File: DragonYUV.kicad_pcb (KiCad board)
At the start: 4 copper layers, 120 x 64.1 mm, 68 parts, among them IC1 74HCT273, IC10 74HCT32, IC12 CD4053, IC2 MC6847, IC3 74HCT00, IC4 74HCT20, IC5 74HCT86, IC6 74HCT393, IC7 74ALS74N, IC8 74HCT393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

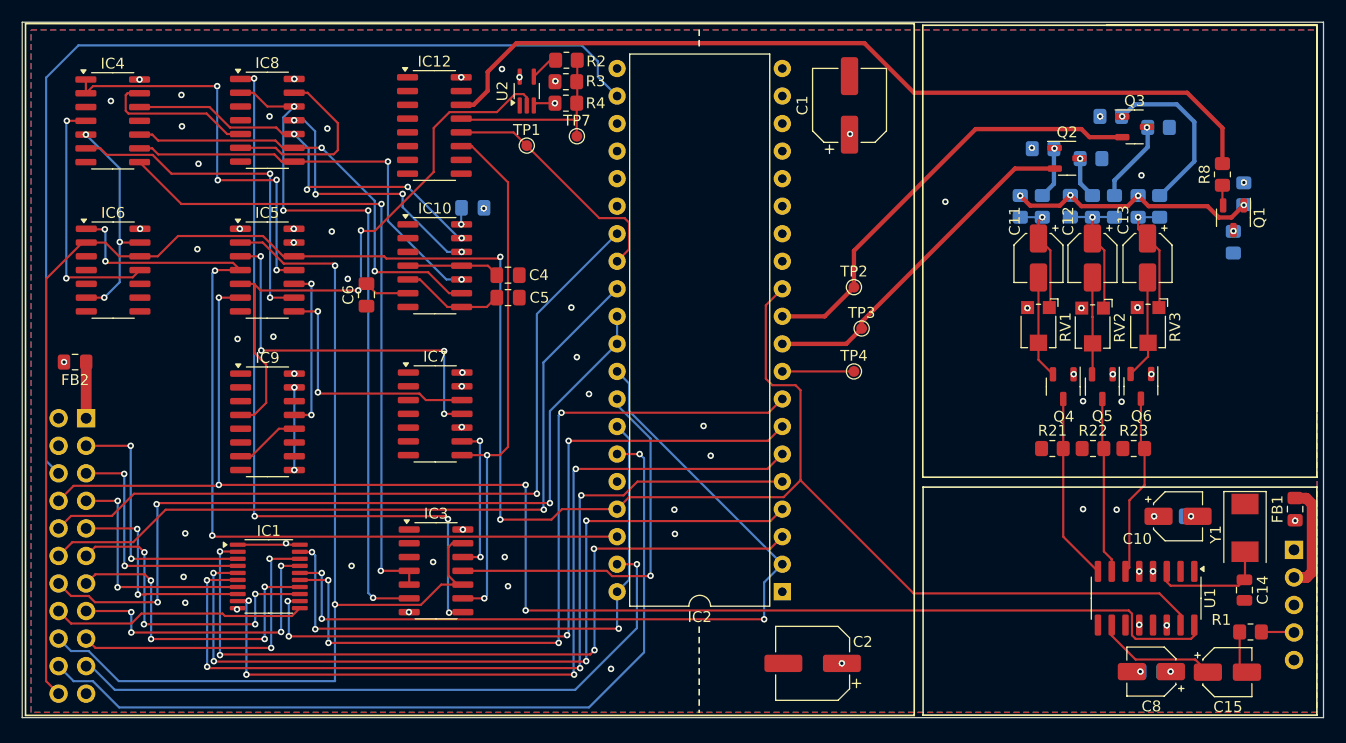
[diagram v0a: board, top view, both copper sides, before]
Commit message: reworked layout
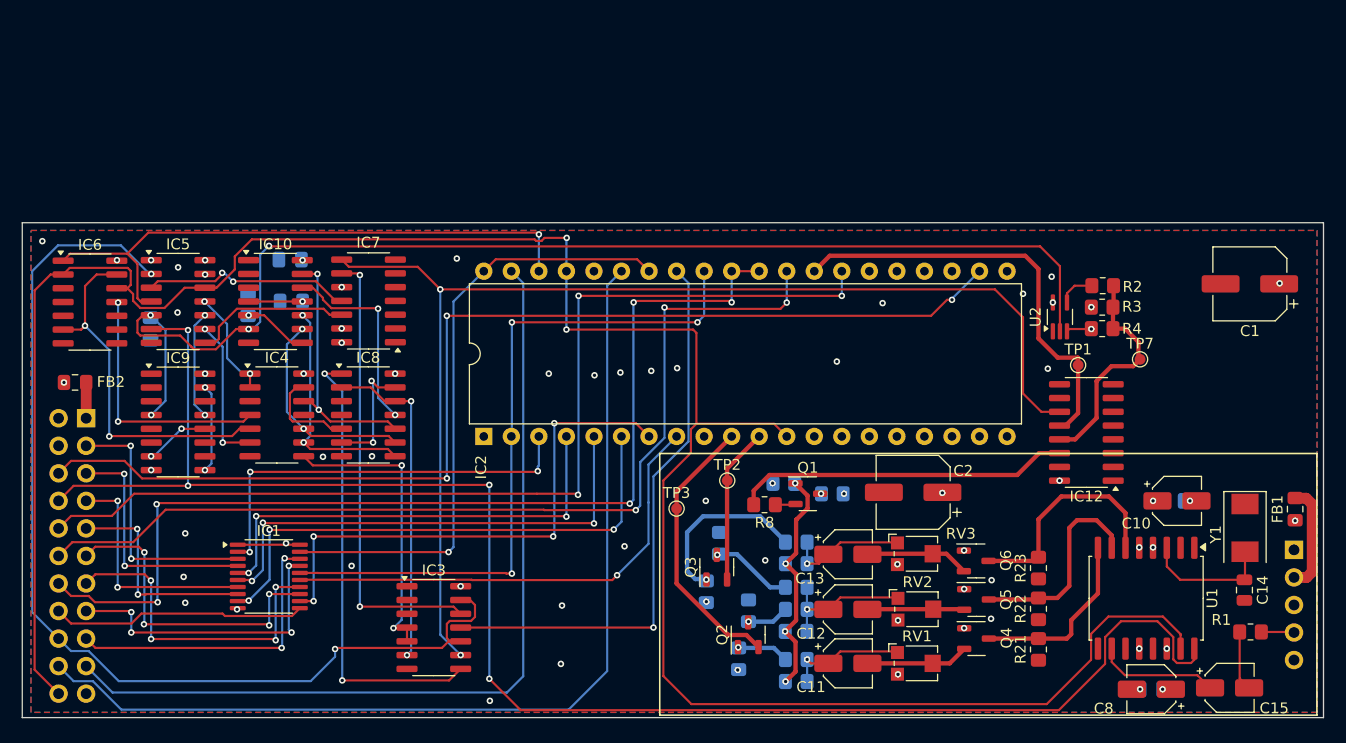
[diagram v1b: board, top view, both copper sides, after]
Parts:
- removed TP4: TestPoint_Chroma, TestPoint:TestPoint_Pad_D1.0mm
- C4, C5, C6: moved to B.Cu
- U1: footprint Package_SO:SOIC-16_3.9x9.9mm_P1.27mm -> Package_SO:SOIC-16W_7.5x10.3mm_P1.27mm
- moved IC12 66.5 mm to (188.2, 100.8), turned to 180 degrees
- moved R12 57.6 mm to (153.1, 115.5), turned to -90 degrees
- moved Q3 56.0 mm to (154.1, 113.3), turned to 90 degrees
- moved TP7 55.9 mm to (193.1, 94.1)
- moved R13 55.8 mm to (154.3, 111.0), turned to -90 degrees
- moved R10 54.8 mm to (156.1, 121.7), turned to -90 degrees
- moved TP1 54.7 mm to (187.4, 94.6)
- moved R3 53.7 mm to (189.6, 89.3)
- moved R4 53.7 mm to (189.6, 91.3)
- moved R2 53.7 mm to (189.7, 87.3)
- moved U2 53.4 mm to (185.7, 90.2)
- moved Q2 52.9 mm to (157.0, 119.5), turned to 90 degrees
- moved R11 52.3 mm to (157.0, 117.3), turned to -90 degrees
- moved R8 52.1 mm to (158.5, 107.5), turned to 180 degrees
- moved R7 50.1 mm to (160.3, 105.5), turned to 180 degrees
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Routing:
- net LUM CONTROL: track 50.0 -> 110.6 mm
- net /LINE PULSES: track 60.1 -> 113.0 mm, vias 2 -> 4
- net MUX X: track 80.1 -> 30.9 mm
- net /Q0: track 73.4 -> 38.3 mm, vias 4 -> 3
- net /Q2: track 80.4 -> 45.7 mm, vias 4 -> 3
- net Net-(IC3-Pad4): track 61.7 -> 27.3 mm
- net /Q1: track 76.3 -> 42.6 mm, vias 4 -> 3
- net Net-(IC8A-MR): track 62.6 -> 30.5 mm, vias 4 -> 2
- net Net-(IC7B-Q): track 14.0 -> 41.9 mm
- net /Q3: track 76.9 -> 49.0 mm, vias 4 -> 3
- net /~{VCLK}: track 69.6 -> 41.9 mm, vias 4 -> 2
- net Net-(IC4-Pad1): track 37.7 -> 10.1 mm, vias 4 -> 2
- net ~{HS}: track 81.8 -> 54.3 mm, vias 4 -> 1
- net /Q5: track 71.9 -> 44.5 mm, vias 4 -> 1
- net phiA: track 40.8 -> 14.4 mm
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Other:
- board size 120 x 64.1 mm -> 120 x 45.6 mm

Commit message: Clean up board Improve trace quality
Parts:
- added TP4: TestPoint_MuxX, TestPoint:TestPoint_Pad_D1.0mm, F.Cu at (180.7, 104.7)
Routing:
- net DO6: track 28.1 -> 30.8 mm
- net CLK: track 52.4 -> 50.7 mm
- net /LINE PULSES: track 113.0 -> 114.3 mm
- net ~{RAS0}: track 23.5 -> 24.8 mm
- net VCLK: track 96.8 -> 95.8 mm
- net DO7: track 28.2 -> 29.0 mm
- net ~{FS}: track 213.6 -> 214.5 mm
- net DO5: track 30.6 -> 31.4 mm
- net DO4: track 29.9 -> 30.6 mm
- net LUM: track 39.9 -> 40.4 mm, vias 0 -> 1
- net GM0: track 95.9 -> 95.3 mm
- net GM1: track 89.3 -> 88.7 mm
- net GND: vias 38 -> 48
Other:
- board text added: "DRAGON REV.3 PAL"

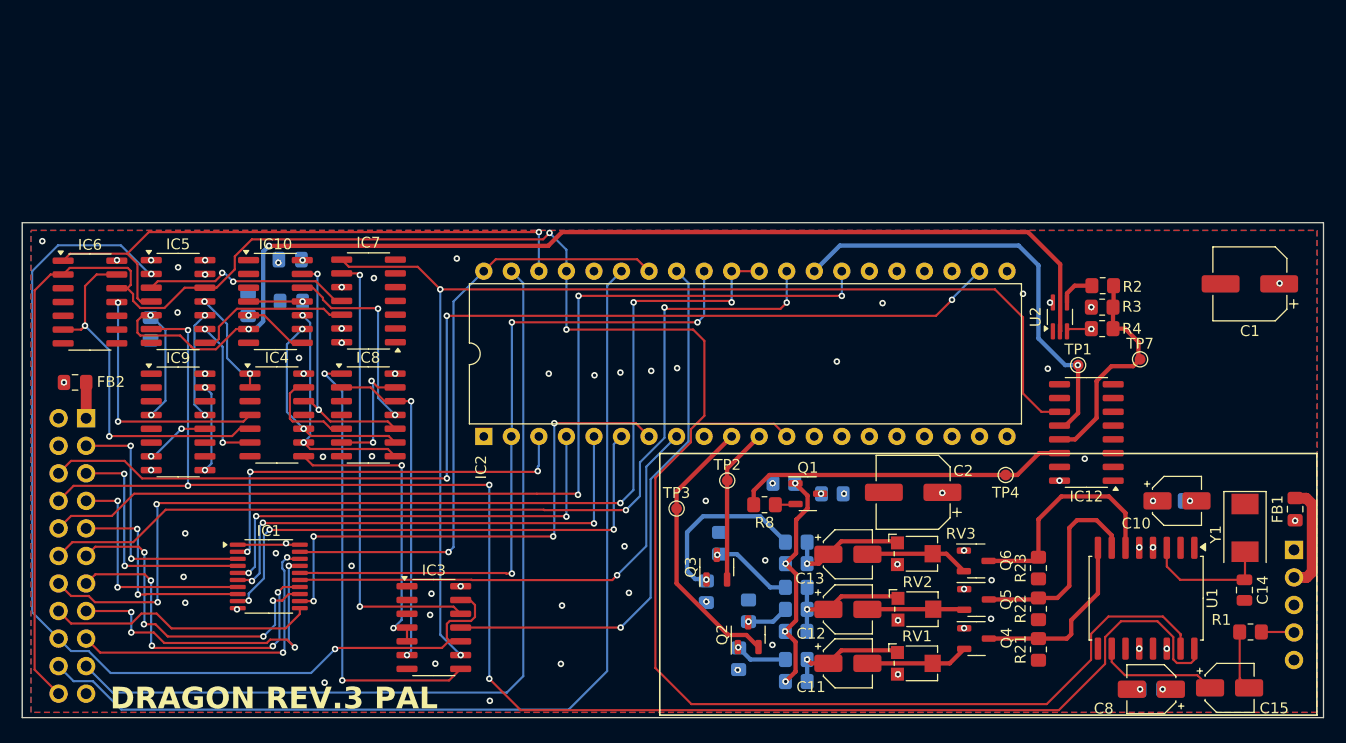
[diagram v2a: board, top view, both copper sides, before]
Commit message: bolster video output routing
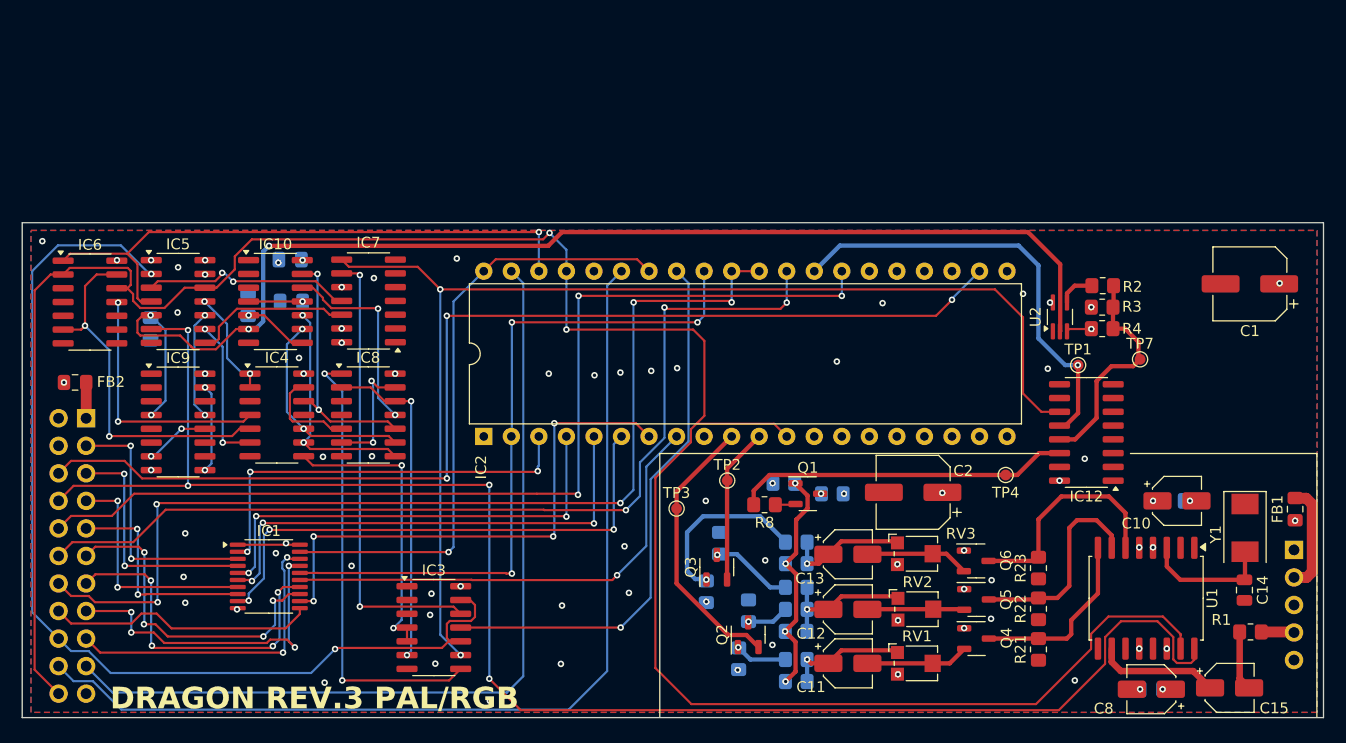
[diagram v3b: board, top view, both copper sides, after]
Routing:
- net ~{FS}: track 214.5 -> 213.9 mm
- net GND: vias 48 -> 49
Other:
- board text added: "DRAGON REV.3 PAL/RGB"
- board text removed: "DRAGON REV.3 PAL"

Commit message: convert to cpld
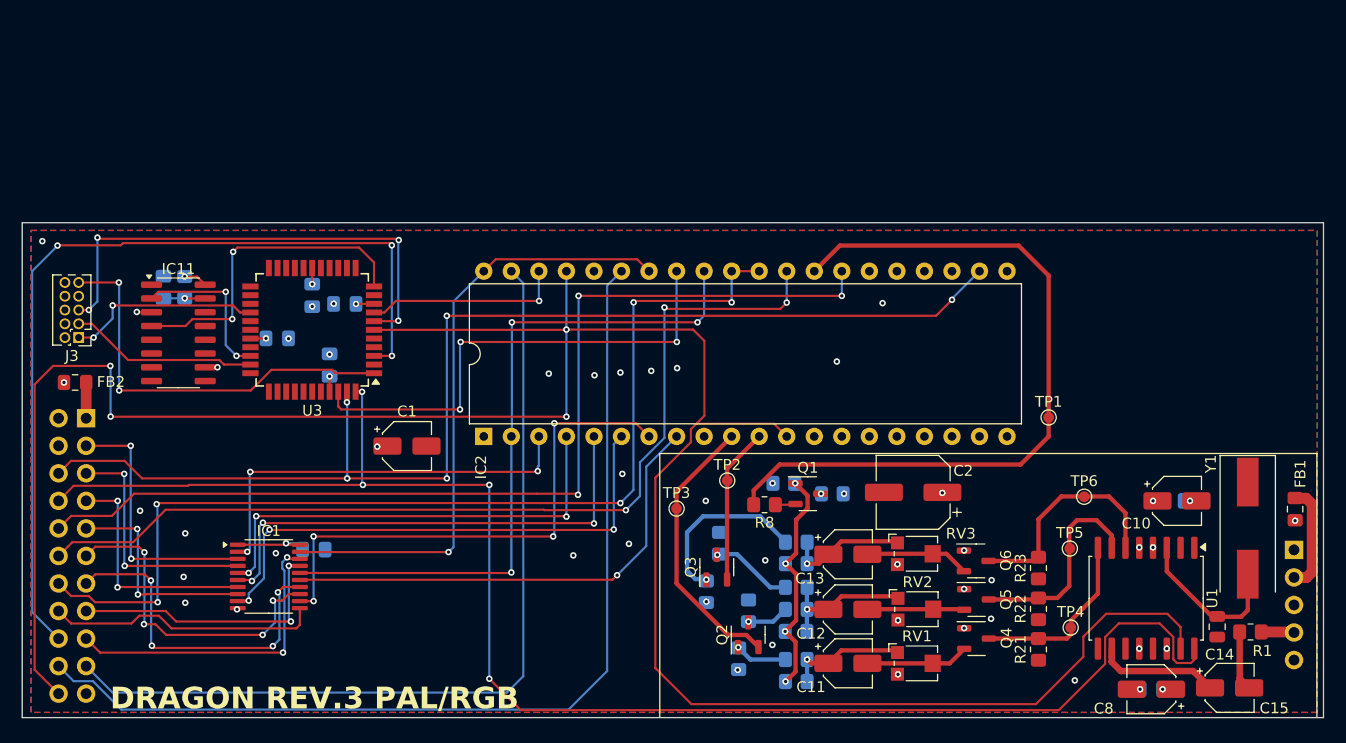
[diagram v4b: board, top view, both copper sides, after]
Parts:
- removed C5: 100pF, Capacitor_SMD:C_0805_2012Metric_Pad1.18x1.45mm_HandSolder
- removed C6: 180pF, Capacitor_SMD:C_0805_2012Metric_Pad1.18x1.45mm_HandSolder
- removed C9: 0.01uF, Capacitor_SMD:C_0805_2012Metric_Pad1.18x1.45mm_HandSolder
- removed IC10: 74HCT32, Package_SO:SOIC-14_3.9x8.7mm_P1.27mm
- removed IC12: CD4053, Package_SO:SOIC-16_3.9x9.9mm_P1.27mm
- removed IC3: 74HCT00, Package_SO:SOIC-14_3.9x8.7mm_P1.27mm
- removed IC4: 74HCT20, Package_SO:SOIC-14_3.9x8.7mm_P1.27mm
- removed IC5: 74HCT86, Package_SO:SOIC-14_3.9x8.7mm_P1.27mm
- removed IC6, IC8: 74HCT393, Package_SO:SOIC-14_3.9x8.7mm_P1.27mm
- removed IC7: 74ALS74N, Package_SO:SOIC-14_3.9x8.7mm_P1.27mm
- removed IC9: 74HCT390, Package_SO:SOIC-16_3.9x9.9mm_P1.27mm
- removed R2: 12K, Resistor_SMD:R_0805_2012Metric_Pad1.20x1.40mm_HandSolder
- removed R3: 8K2, Resistor_SMD:R_0805_2012Metric_Pad1.20x1.40mm_HandSolder
- removed R4: 1K8, Resistor_SMD:R_0805_2012Metric_Pad1.20x1.40mm_HandSolder
- removed TP7: TestPoint_LinePulse, TestPoint:TestPoint_Pad_D1.0mm
- removed U2: 74AHC1G04, Package_TO_SOT_SMD:SOT-353_SC-70-5_Handsoldering
- added C16: 0.1uF, Capacitor_SMD:C_0805_2012Metric_Pad1.18x1.45mm_HandSolder, B.Cu at (116.8, 88.2)
- added C17: 0.1uF, Capacitor_SMD:C_0805_2012Metric_Pad1.18x1.45mm_HandSolder, B.Cu at (113.5, 92.2)
- added C18: 0.1uF, Capacitor_SMD:C_0805_2012Metric_Pad1.18x1.45mm_HandSolder, B.Cu at (118.4, 94.6)
- added C19: 0.1uF, Capacitor_SMD:C_0805_2012Metric_Pad1.18x1.45mm_HandSolder, B.Cu at (119.8, 89.0)
- added C20: 330pF, Capacitor_SMD:C_0805_2012Metric_Pad1.18x1.45mm_HandSolder, B.Cu at (103.0, 87.5)
- added IC11: 74LS123N, Package_SO:SOIC-16_3.9x9.9mm_P1.27mm, F.Cu at (104.4, 91.6)
- added J3: JTAG, Connector_PinHeader_1.27mm:PinHeader_2x05_P1.27mm_Vertical, F.Cu at (95.2, 92.1)
- added R5: 27K, Resistor_SMD:R_0805_2012Metric_Pad1.20x1.40mm_HandSolder, B.Cu at (105.0, 87.5)
- added TP5: TestPoint_Green, TestPoint:TestPoint_Pad_D1.0mm, F.Cu at (186.6, 111.5)
- added TP6: TestPoint_Blue, TestPoint:TestPoint_Pad_D1.0mm, F.Cu at (188.0, 106.8)
- added U3: ATF1504ASL-xAx44, Package_QFP:TQFP-44_10x10mm_P0.8mm, F.Cu at (116.8, 91.4)
- C1: footprint Capacitor_SMD:CP_Elec_6.3x5.8 -> Capacitor_SMD:CP_Elec_4x5.4
- C14: value 52pF -> 51pF
- C4: value 180pF -> 0.1uF
- TP4: value TestPoint_MuxX -> TestPoint_Blue
- Y1: footprint Crystal:Crystal_SMD_0603-2Pin_6.0x3.5mm -> Crystal:Crystal_SMD_HC49-SD
- moved C1 79.2 mm to (125.5, 102.1), turned to 0 degrees
- moved C4 23.0 mm to (116.9, 111.6)
- moved TP4 15.3 mm to (186.7, 118.8)
- moved TP1 5.54 mm to (184.7, 99.4)
- moved C14 4.21 mm to (200.2, 118.7)
- moved Y1 0.26 mm to (203.0, 109.7)
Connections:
- C4 pad 1: Net-(C4-Pad1) -> GND
- C4 pad 2: GND -> +5V
- R8 pad 2: MUX X -> LUM
- TP4 pad 1: MUX X -> BLUE
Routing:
- net /LINE PULSES: track 114.3 -> 0.00 mm, vias 4 -> 0
- net LUM CONTROL: track 110.6 -> 0.00 mm, vias 2 -> 0
- net TMS: track 0.00 -> 45.5 mm, vias 0 -> 4
- net Net-(IC7B-Q): track 41.9 -> 0.00 mm, vias 2 -> 0
- net /~{VCLK}: track 41.9 -> 0.00 mm, vias 2 -> 0
- net TDI: track 0.00 -> 38.1 mm, vias 0 -> 2
- net ~{HS}: track 54.5 -> 18.4 mm
- net Net-(IC6A-Q3): track 33.6 -> 0.00 mm, vias 2 -> 0
- net MUX X: track 30.9 -> 0.00 mm
- net Net-(IC8A-MR): track 30.5 -> 0.00 mm, vias 2 -> 0
- net PhaseT: track 0.00 -> 29.9 mm, vias 0 -> 2
- net LUM: track 40.4 -> 69.2 mm, vias 1 -> 0
- net Net-(IC3-Pad4): track 27.3 -> 0.00 mm, vias 2 -> 0
- net Net-(IC6B-Q0): track 23.5 -> 0.00 mm, vias 2 -> 0
- net /~{VCLK}/32: track 23.5 -> 0.00 mm, vias 2 -> 0
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
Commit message: update design to provide ntsc and pal switching
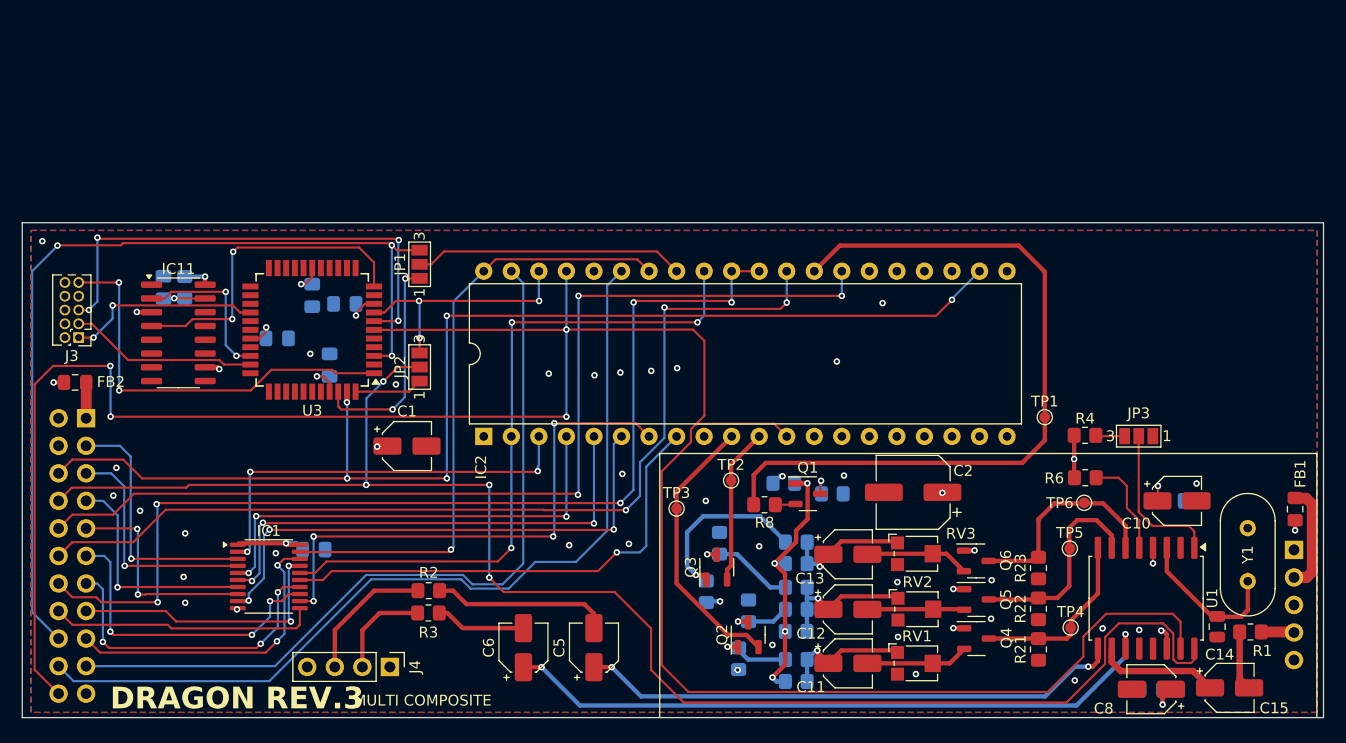
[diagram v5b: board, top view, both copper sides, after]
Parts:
- added C5: 220uF, Capacitor_SMD:CP_Elec_4x5.4, F.Cu at (142.7, 120.7)
- added C6: 220uF, Capacitor_SMD:CP_Elec_4x5.4, F.Cu at (136.2, 120.7)
- added J4: SVid, Connector_PinHeader_2.54mm:PinHeader_1x04_P2.54mm_Vertical, F.Cu at (123.9, 122.5)
- added JP1: Video Clock, Jumper:SolderJumper-3_P1.3mm_Open_Pad1.0x1.5mm_NumberLabels, F.Cu at (126.7, 85.3)
- added JP2: Video HS, Jumper:SolderJumper-3_P1.3mm_Open_Pad1.0x1.5mm_NumberLabels, F.Cu at (126.7, 94.8)
- added JP3: Video Format, Jumper:SolderJumper-3_P1.3mm_Open_Pad1.0x1.5mm_NumberLabels, F.Cu at (193.0, 101.2)
- added R2: 75R, Resistor_SMD:R_0805_2012Metric_Pad1.20x1.40mm_HandSolder, F.Cu at (127.5, 115.4)
- added R3: 75R, Resistor_SMD:R_0805_2012Metric_Pad1.20x1.40mm_HandSolder, F.Cu at (127.5, 117.5)
- added R4: 10K, Resistor_SMD:R_0805_2012Metric_Pad1.20x1.40mm_HandSolder, F.Cu at (188.0, 101.1)
- added R6: 10K, Resistor_SMD:R_0805_2012Metric_Pad1.20x1.40mm_HandSolder, F.Cu at (188.1, 105.0)
- C15: value 10uF -> 220uF
- U1: value AD724RJ -> AD724JR
- Y1: footprint Crystal:Crystal_SMD_HC49-SD -> Crystal:Crystal_HC18-U_Vertical
- moved TP6 0.56 mm to (188.0, 107.3)
- moved TP1 0.36 mm to (184.3, 99.4)
- moved TP2 0.36 mm to (155.4, 105.3)
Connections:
- U1 pad 1: GND -> Net-(JP3-C)
- U1 pad 11: unconnected-(U1-LUM_OUT-Pad11) -> Net-(U1-LUM_OUT)
- U1 pad 5: +5V -> Net-(U1-CE)
- U1 pad 9: unconnected-(U1-CHROM_OUT-Pad9) -> Net-(U1-CHROM_OUT)
- U3 pad 42: CLK -> CLK'
- U3 pad 44: ~{NHS} -> ~{HS'}
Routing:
- net Net-(U1-LUM_OUT): track 0.00 -> 62.6 mm, vias 0 -> 2
- net Net-(U1-CHROM_OUT): track 0.00 -> 50.1 mm, vias 0 -> 2
- net +5V: track 20.0 -> 48.4 mm
- net CLK: track 45.4 -> 24.4 mm, vias 3 -> 0
- net CLK': track 0.00 -> 20.9 mm, vias 0 -> 2
- net Net-(C5-Pad2): track 0.00 -> 16.9 mm
- net Net-(JP3-C): track 0.00 -> 14.4 mm
- net CHROMA OUT: track 0.00 -> 12.6 mm
- net Net-(U1-CE): track 0.00 -> 9.32 mm
- net LUMA OUT: track 0.00 -> 9.14 mm
- net ~{A}/G: track 91.2 -> 82.1 mm
- net Net-(C6-Pad2): track 0.00 -> 8.34 mm
- net CSS: track 79.8 -> 72.4 mm
- net ~{HS'}: track 0.00 -> 6.31 mm
- net ~{HS}: track 18.4 -> 23.2 mm, vias 1 -> 3
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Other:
- board text added: "DRAGON REV.3"
- board text added: "MULTI COMPOSITE"
- board text removed: "DRAGON REV.3 PAL/RGB"
